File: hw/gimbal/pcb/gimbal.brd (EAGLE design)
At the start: 60 x 42 mm, 75 parts

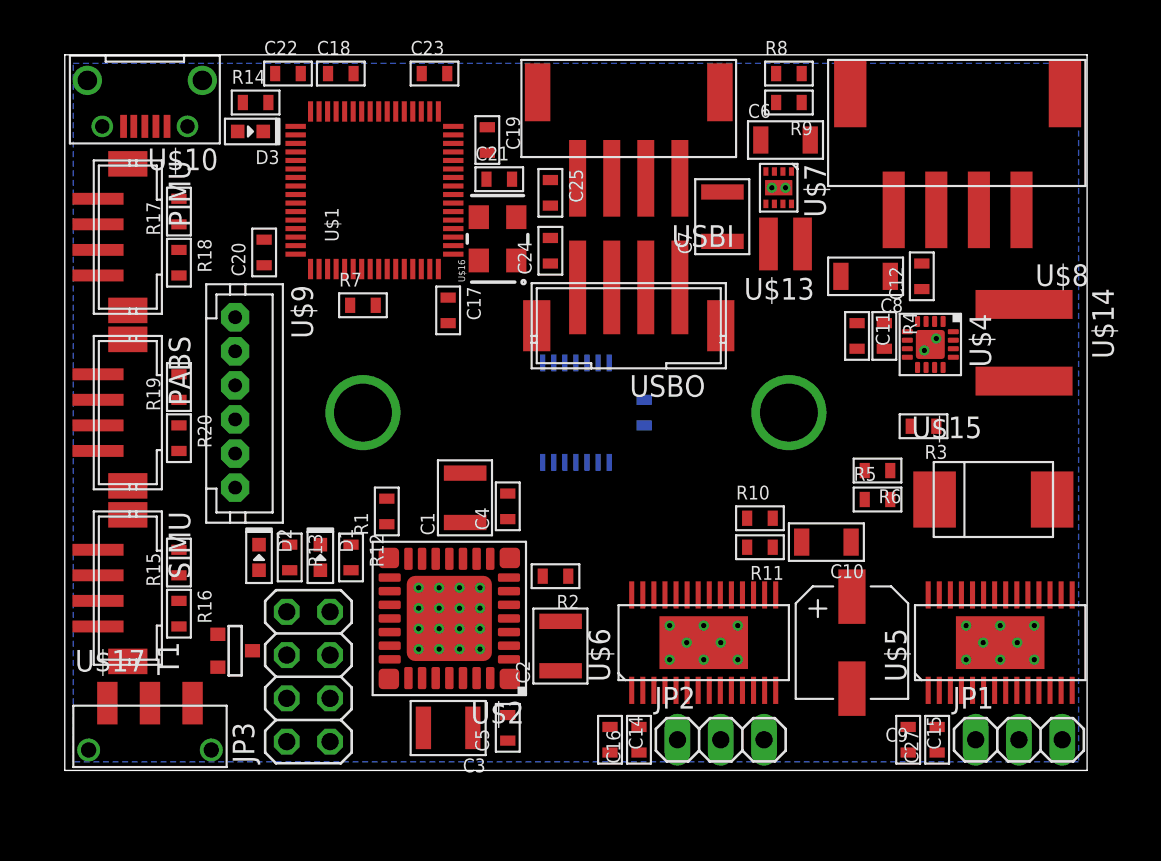
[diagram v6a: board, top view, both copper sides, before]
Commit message: gimbal board: Work towards naming all components.
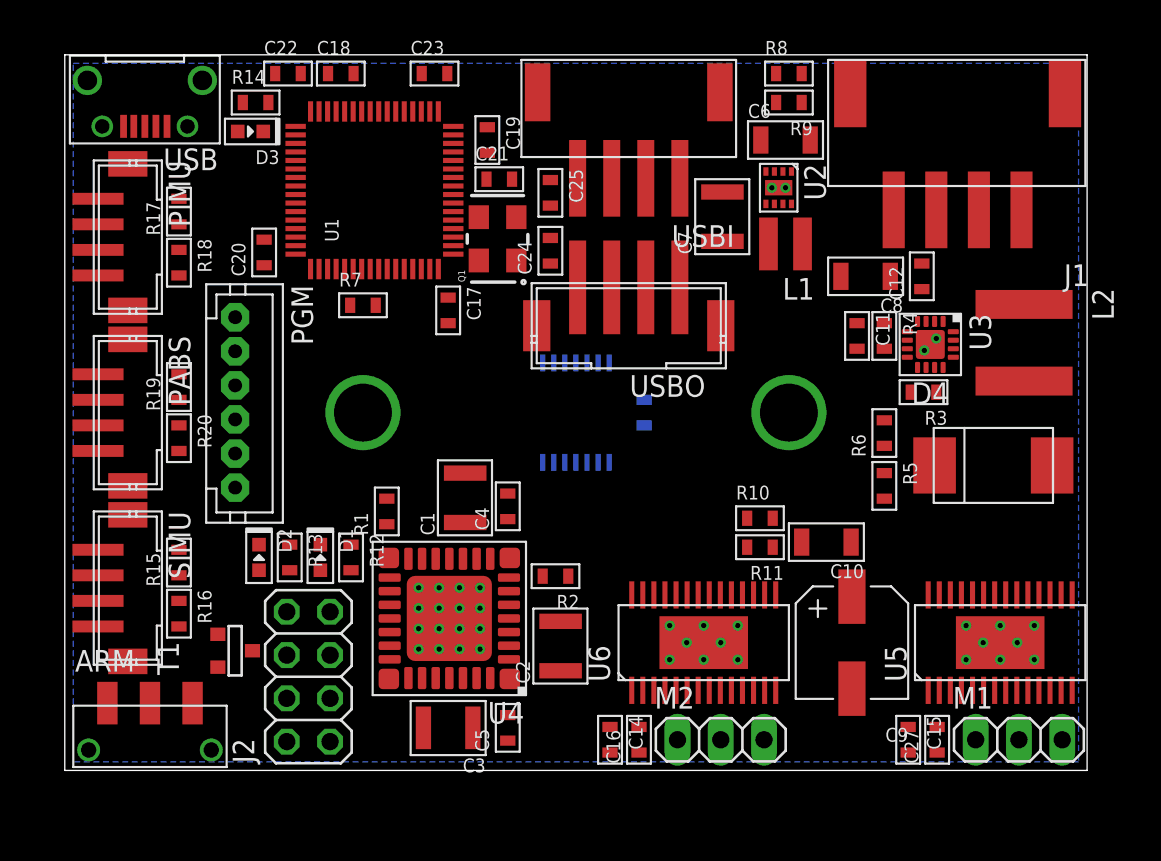
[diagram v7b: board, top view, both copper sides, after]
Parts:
- removed U$15: DIODEB520C, gimbal:B520C
- added D4: DIODEB520C, gimbal:B520C
- moved R6 2.24 mm to (48.1, 19.8), turned to 90 degrees
- moved R3 2.00 mm to (50.4, 22.2)
- moved R5 0.89 mm to (48.1, 16.7), turned to 270 degrees
- renumbered JP1 to M1, JP2 to M2, JP3 to J2, U$1 to U1, U$10 to USB, U$11 to MOUNT1, U$12 to MOUNT2, U$13 to L1, U$14 to L2, U$16 to Q1, U$17 to ARM, U$2 to U4, U$3 to U7, U$4 to U3, U$5 to U5, U$6 to U6, U$7 to U2, U$8 to J1, U$9 to PGM
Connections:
- net +12V: now also D4.1; no longer U$15.1
- net N$17: now also D4.2; no longer U$15.2

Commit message: gimbal board: Rename all components and move around parts in the schematic to be slightly more organized.
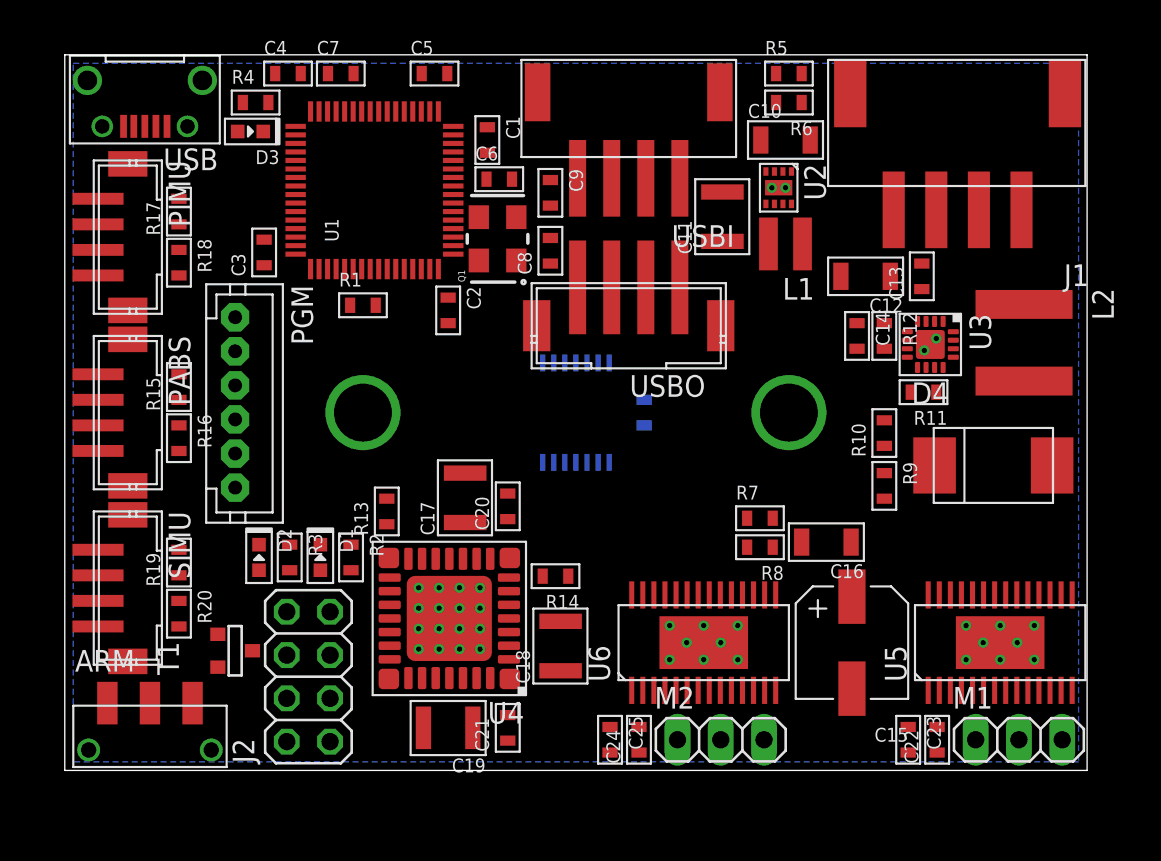
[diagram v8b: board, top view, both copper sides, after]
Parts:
- removed C27: 0.1uF, mfpassives:C0603
- added C26: 0.1uF, mfpassives:C0603
- C1, C7: value 22uF 16V -> 4.7uF; device mfpassives:C1210 -> mfpassives:C0603
- C11, C17: value 0.1uF -> 22uF 16V; device mfpassives:C0603 -> mfpassives:C1210
- C12: value 0.047uF -> 10uF; device mfpassives:C0603 -> mfpassives:C1206
- C13: value 0.1uF -> 0.047uF
- C14: value 0.01uF -> 0.1uF
- C15: value 0.01uF -> 100uF; device mfpassives:C0603 -> mfpassives:CP6.3MM
- C16: value 0.1uF -> 10uF; device mfpassives:C0603 -> mfpassives:C1206
- C18, C19: value 4.7uF -> 22uF 16V; device mfpassives:C0603 -> mfpassives:C1210
- C2, C3: value 22uF 16V -> 0.1uF; device mfpassives:C1210 -> mfpassives:C0603
- C23: value 0.1uF -> 0.01uF
- C24: value 10pF -> 0.1uF
- C25: value 10pF -> 0.01uF
- C6: value 10uF -> 0.1uF; device mfpassives:C1206 -> mfpassives:C0603
- C8: value 10uF -> 10pF; device mfpassives:C1206 -> mfpassives:C0603
- C9: value 100uF -> 10pF; device mfpassives:CP6.3MM -> mfpassives:C0603
- R1: value 100k -> 10
- R10, R8: value 100k -> 10k
- R11: value 10k -> 78.4k
- R12: value 560 -> 1.87k
- R13: value 560 -> 100k
- R14: value 560 -> 220
- R2: value 220 -> 560
- R3: value 78.4k -> 560
- R4: value 1.87k -> 560
- R5: value 88k -> 100k
- R7: value 10 -> 100k
- R9: value 10k -> 88k
- moved C22 54.6 mm to (51.2, 1.80), turned to 90 degrees
- moved C23 48.0 mm to (49.5, 1.80), turned to 270 degrees
- moved R4 39.4 mm to (11.2, 39.2), turned to 0 degrees
- moved C5 38.6 mm to (21.7, 40.9), turned to 0 degrees
- moved R3 38.4 mm to (13.2, 12.5), turned to 270 degrees
- moved C18 36.0 mm to (29.1, 7.30), turned to 90 degrees
- moved C19 34.6 mm to (22.5, 2.50), turned to 180 degrees
- moved R12 33.9 mm to (48.1, 25.5)
- moved R14 32.9 mm to (28.8, 11.4), turned to 180 degrees
- moved C25 32.3 mm to (32.0, 1.80)
- moved C21 32.2 mm to (26.0, 2.50), turned to 90 degrees
- moved C9 31.8 mm to (28.5, 33.9), turned to 270 degrees
- moved C3 29.9 mm to (11.7, 30.4), turned to 90 degrees
- moved C24 29.2 mm to (33.7, 1.80)
- moved C4 28.5 mm to (13.1, 40.9), turned to 0 degrees
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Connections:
- net +12V: now also C15.P$1, C22.P$1, C24.P$1, R7.P$2, R9.P$2; no longer C10.P$1, C27.P$1, C9.P$1, R10.P$2, R5.P$2
- net +3V3: now also C1.P$1, C11.P$1, C2.P$1, C26.P$1, C3.P$1, C4.P$1, C5.P$1, R2.P$2, R3.P$2, R4.P$2; no longer C13.P$1, C17.P$1, C19.P$1, C20.P$1, C22.P$1, C23.P$1, C7.P$1, R1.P$2, R12.P$2, R14.P$2
- net +8V: now also C10.P$1, C12.P$1, C17.P$1, C18.P$1, C19.P$1, C20.P$1, C21.P$1, R5.P$2; no longer C1.P$1, C2.P$1, C3.P$1, C4.P$1, C5.P$1, C6.P$1, C8.P$1, R8.P$2
- net GND: now also C14.P$2, C15.P$2, C16.P$2, C26.P$2, C5.P$2, R1.P$1, R10.P$1, R14.P$1, R8.P$1; no longer C21.P$2, C22.P$2, C23.P$2, C24.P$2, C25.P$2, R2.P$1, R3.P$1, R7.P$1, R9.P$1
- net MOTOR_FB: now also R14.P$2; no longer R2.P$2
- net MOTOR_SF: now also R13.P$1; no longer R1.P$1
- net N$18: now also R11.P$2; no longer R3.P$2
- net N$19: now also C14.P$1, R12.P$1; no longer C11.P$1, R4.P$1
- net N$20: now also R12.P$2; no longer R4.P$2
- net N$21: now also C13.P$1; no longer C12.P$1
- net N$22: now also R10.P$2, R9.P$1; no longer R5.P$1, R6.P$2
- net N$23: now also C7.P$1; no longer C18.P$1
- net N$24: now also C6.P$1; no longer C21.P$1
- net N$25: now also C25.P$1; no longer C14.P$1
- net N$26: now also C25.P$2; no longer C14.P$2
- net N$27: now also C23.P$2; no longer C15.P$2
- net N$28: now also C23.P$1; no longer C15.P$1
- net N$29: now also C22.P$2; no longer C27.P$2
- net N$30: now also C24.P$2; no longer C16.P$2
- net N$33: now also R1.P$2; no longer R7.P$2
- net N$34: now also R5.P$1, R6.P$2; no longer R8.P$1, R9.P$2
- net N$35: now also C8.P$1; no longer C24.P$1
- net N$36: now also C9.P$1; no longer C25.P$1
- net N$38: now also R7.P$1, R8.P$2; no longer R10.P$1, R11.P$2
- net N$39: now also R2.P$1; no longer R12.P$1
- net N$40: now also R3.P$1; no longer R13.P$1
- net N$41: now also R4.P$1; no longer R14.P$1
- net N$5: now also C21.P$2; no longer C5.P$2
- net PABS_SCL: now also R16.P$1; no longer R20.P$1
- net PABS_SDA: now also R15.P$1; no longer R19.P$1
- net SIMU_SCL: now also R20.P$1; no longer R16.P$1
- net SIMU_SDA: now also R19.P$1; no longer R15.P$1
